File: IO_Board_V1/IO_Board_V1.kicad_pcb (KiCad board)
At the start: 2 copper layers, 79 x 49.5 mm, 92 parts, among them J1 USB_C_Receptacle_USB2.0, J10 IFM1, J11 FOURCHE, J12 BTN, J13 FOURCHE, J14 BTN, J15 CON_UART, J16 BTN, J17 FOURCHE, J18 IFM2, J19 IFM3, J2 CON_debug, J20 FOURCHE, J21 CON_I2C, J22 IFM4, J23 SPI, J24 BTN, J3 Conn_ARM_JTAG_SWD_10, J4 CON_CAN, J5 CON_CAN, J6 12V, J7 BTN, J8 BTN, J9 IFM0, SW1 BOOT, SW2 RST, U1 STM32F302C6Tx, U2 NCP1117-3.3_SOT223, U3 SN65HVD232, Y1 8MHz

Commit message: change connector and some final touch
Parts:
- J4, J5: footprint AREA_lib_Connector:Wuerth_2mm_4pin_62000411622 -> AREA_lib_Connector:690367290476
- moved CANL1 4.43 mm to (94.8, 122.3), turned to 180 degrees
- moved CANH1 2.31 mm to (94.9, 117.8), turned to 180 degrees
- moved J5 0.53 mm to (88.8, 126.5)
- renumbered JP1 to 120
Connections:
- J3 pad 4: /SWCLK -> /CLK
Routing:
- net /CANL: track 44.4 -> 56.0 mm
- net /CANH: track 50.3 -> 39.8 mm
- net +5V: track 185.9 -> 177.7 mm, vias 0 -> 3
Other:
- board text added: "12V"
- board text added: "3.3V"
- board text added: "CLK"
- board text added: "GND"
- board text added: "IFM1"
- board text added: "IFM2"
- board text added: "IFM3"
- board text added: "IFM4"
- board text added: "MISO"
- board text added: "MOSI"
- board text added: "RX"
- board text added: "S"
- board text added: "SPI"
- board text added: "TX"
- board text added: "UART1"

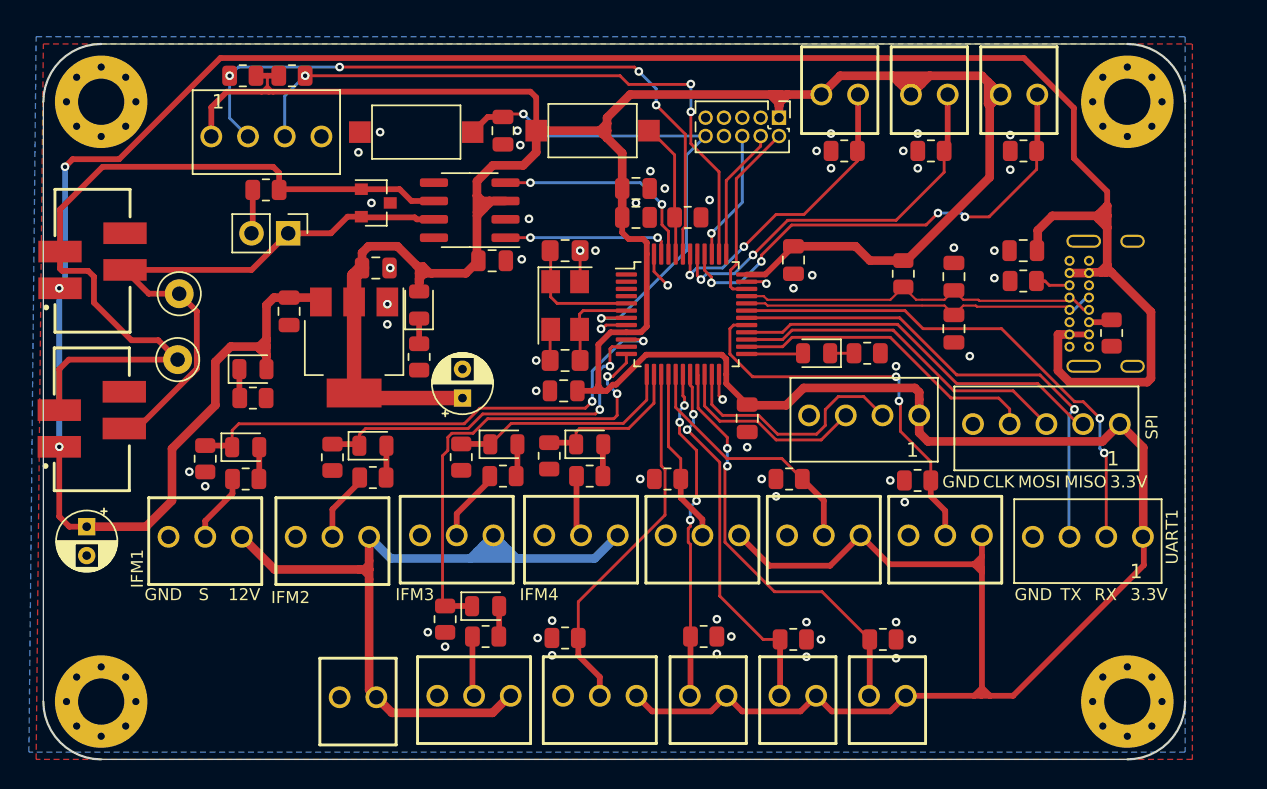
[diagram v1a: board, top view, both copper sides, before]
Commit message: esp32 pas fini + silkscreen  IO ok
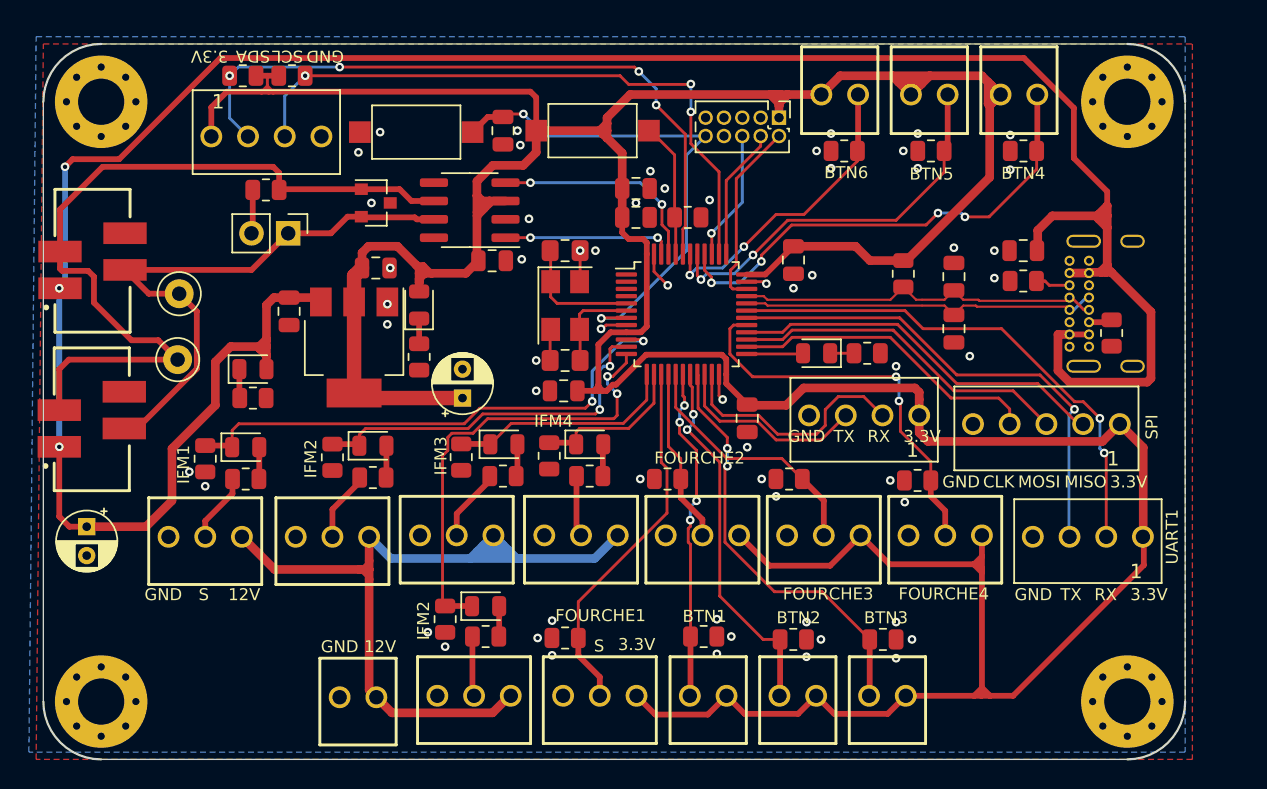
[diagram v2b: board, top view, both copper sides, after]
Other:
- board text added: "BTN1"
- board text added: "BTN2"
- board text added: "BTN3"
- board text added: "BTN4"
- board text added: "BTN5"
- board text added: "BTN6"
- board text added: "FOURCHE1"
- board text added: "FOURCHE2"
- board text added: "FOURCHE3"
- board text added: "FOURCHE4"
- board text added: "SCL"
- board text added: "SDA"
